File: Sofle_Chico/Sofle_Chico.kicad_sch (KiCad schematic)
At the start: 114 parts, among them J1 Conn_01x05, J2 MJ-4PP-9, J3 Conn_01x04, J4 Conn_01x04, J5 Conn_01x05, J6 Conn_01x05, J7 Conn_01x04, Q1 DMG2305UX, SW1 SW_PUSH, SW10 SW_PUSH, SW11 SW_PUSH, SW12 SW_PUSH, SW13 SW_PUSH, SW14 SW_PUSH, SW15 SW_PUSH, SW16 SW_PUSH, SW17 SW_PUSH, SW18 SW_PUSH, SW19 SW_PUSH, SW2 SW_PUSH, SW20 SW_PUSH, SW21 SW_PUSH, SW22 SW_PUSH, SW23 SW_PUSH, SW24 SW_PUSH, SW25 Rotary_Encoder_Switch-Device, SW26 SW_PUSH, SW27 SW_PUSH, SW28 SW_PUSH, SW29 SW_PUSH, SW3 SW_PUSH, SW30 SW_PUSH, SW4 SW_PUSH, SW5 SW_PUSH, SW6 SW_PUSH, SW7 SW_PUSH, SW8 SW_PUSH, SW9 SW_PUSH, U1 SN74AHCT1G125, U2 Pico

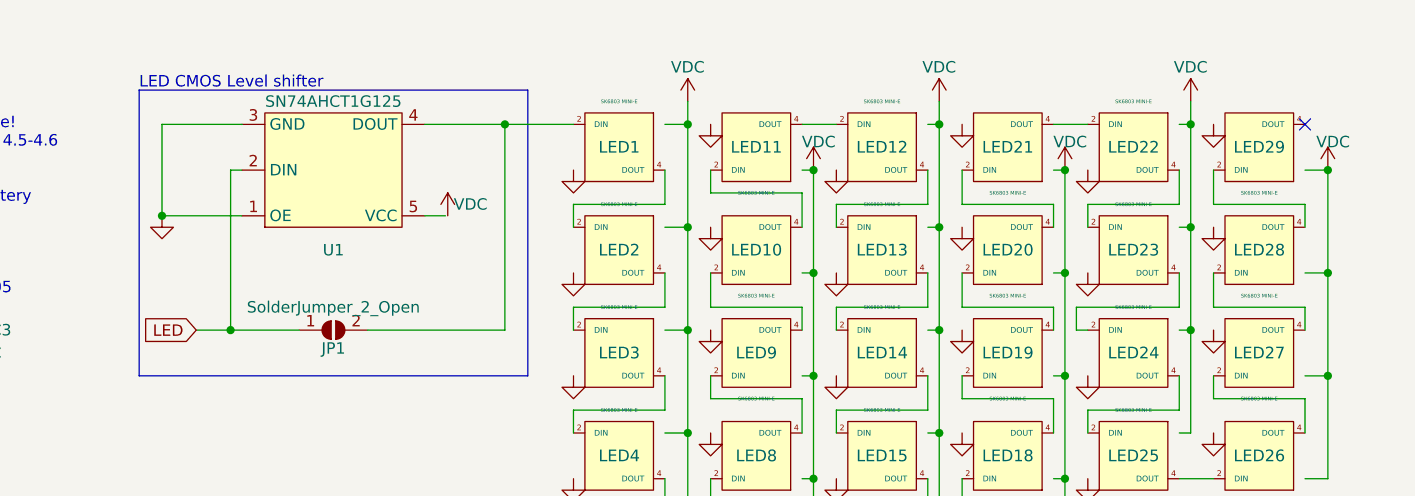
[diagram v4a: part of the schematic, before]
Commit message: Layout progress
LAYOUT PROGRESS
Abandoned Choc V2 support, just aint worth the thru-holes.
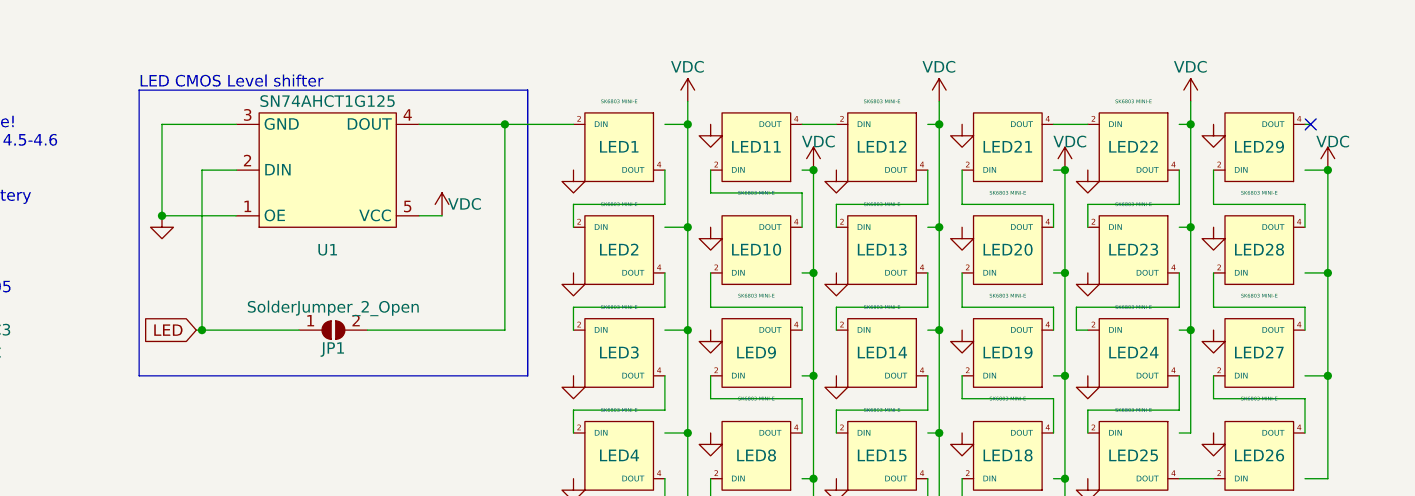
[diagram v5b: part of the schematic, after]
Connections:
- net VDC: now also U1.5 (VCC)
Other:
- moved on the sheet: U1
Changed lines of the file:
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@@
   (junction (at 204.47 123.19) (diameter 0) (color 0 0 0 0)
   )
+  (junction (at 133.985 48.26) (diameter 0) (color 0 0 0 0)
+  )
   (junction (at 215.9 59.69) (diameter 0) (color 0 0 0 0)
   )
@@
   (junction (at 240.03 114.3) (diameter 0) (color 0 0 0 0)
   )
-  (junction (at 137.16 48.26) (diameter 0) (color 0 0 0 0)
-  )
   (junction (at 143.51 139.7) (diameter 0) (color 0 0 0 0)
   )
@@
   (no_connect (at 69.85 166.37))
   (no_connect (at 48.26 78.74))
-  (no_connect (at 256.54 25.4))
+  (no_connect (at 257.175 25.4))
   (wire (pts (xy 214.63 76.2) (xy 218.44 76.2))
     (stroke (width 0) (type default))
@@
     (stroke (width 0) (type default))
   )
-  (wire (pts (xy 137.16 48.26) (xy 133.35 48.26))
+  (wire (pts (xy 133.985 48.26) (xy 144.78 48.26))
     (stroke (width 0) (type default))
   )
@@
     (stroke (width 0) (type default))
   )
-  (wire (pts (xy 137.16 30.48) (xy 137.16 48.26))
+  (wire (pts (xy 133.985 30.48) (xy 133.985 48.26))
     (stroke (width 0) (type default))
   )
@@
     (stroke (width 0) (type default))
   )
-  (wire (pts (xy 129.54 25.4) (xy 138.43 25.4))
+  (wire (pts (xy 129.54 25.4) (xy 137.795 25.4))
     (stroke (width 0) (type default))
   )
@@
     (stroke (width 0) (type default))
   )
+  (wire (pts (xy 158.115 35.56) (xy 160.655 35.56))
+    (stroke (width 0) (type default))
+  )
   (wire (pts (xy 256.54 55.88) (xy 246.38 55.88))
     (stroke (width 0) (type default))
@@
     (stroke (width 0) (type default))
   )
-  (wire (pts (xy 161.036 35.56) (xy 158.75 35.56))
-    (stroke (width 0) (type default))
-  )
   (wire (pts (xy 214.63 53.34) (xy 214.63 57.15))
     (stroke (width 0) (type default))
@@
     (stroke (width 0) (type default))
   )
-  (wire (pts (xy 158.75 25.4) (xy 167.64 25.4))
+  (wire (pts (xy 158.115 25.4) (xy 167.64 25.4))
     (stroke (width 0) (type default))
   )
@@
     (stroke (width 0) (type default))
   )
-  (wire (pts (xy 138.43 30.48) (xy 137.16 30.48))
+  (wire (pts (xy 137.795 30.48) (xy 133.985 30.48))
+    (stroke (width 0) (type default))
+  )
+  (wire (pts (xy 257.175 25.4) (xy 256.54 25.4))
     (stroke (width 0) (type default))
   )
@@
     (stroke (width 0) (type default))
   )
+  (wire (pts (xy 133.985 48.26) (xy 133.35 48.26))
+    (stroke (width 0) (type default))
+  )
   (wire (pts (xy 224.79 139.7) (xy 224.79 156.21))
     (stroke (width 0) (type default))
@@
     (stroke (width 0) (type default))
   )
-  (wire (pts (xy 144.78 48.26) (xy 137.16 48.26))
-    (stroke (width 0) (type default))
-  )
   (wire (pts (xy 219.71 130.81) (xy 240.03 130.81))
     (stroke (width 0) (type default))
@@
     (stroke (width 0) (type default))
   )
-  (wire (pts (xy 129.54 35.56) (xy 138.43 35.56))
+  (wire (pts (xy 129.54 35.56) (xy 137.795 35.56))
     (stroke (width 0) (type default))
   )
@@
     )
   )
-  (symbol (lib_id "Sofle_Pico:SN74AHCT1G125") (at 148.59 30.48 0) (mirror x) (unit 1)
+  (symbol (lib_id "Sofle_Pico:SN74AHCT1G125") (at 147.955 30.48 0) (mirror x) (unit 1)
     (in_bom yes) (on_board yes) (dnp no)
-    (property "Reference" "U1" (at 148.59 39.37 0)
+    (property "Reference" "U1" (at 147.955 39.37 0)
       (effects (font (size 1.27 1.27)))
     )
-    (property "Value" "SN74AHCT1G125" (at 148.59 22.86 0)
+    (property "Value" "SN74AHCT1G125" (at 147.955 22.86 0)
       (effects (font (size 1.27 1.27)))
     )
-    (property "Footprint" "PCM_Package_TO_SOT_SMD_AKL:SOT-23-5_HandSoldering" (at 148.59 20.32 0)
+    (property "Footprint" "PCM_Package_TO_SOT_SMD_AKL:SOT-23-5_HandSoldering" (at 147.955 20.32 0)
       (effects (font (size 1.27 1.27)) hide)
     )
-    (property "Datasheet" "https://www.ti.com/general/docs/suppproductinfo.tsp?distId=26&gotoUrl=http%3A%2F%2Fwww.ti.com%2Flit%2Fgpn%2Fsn74ahct1g125" (at 148.59 16.51 0)
+    (property "Datasheet" "https://www.ti.com/general/docs/suppproductinfo.tsp?distId=26&gotoUrl=http%3A%2F%2Fwww.ti.com%2Flit%2Fgpn%2Fsn74ahct1g125" (at 147.955 16.51 0)
       (effects (font (size 1.27 1.27)) hide)
     )
@@
     )
   )
-  (symbol (lib_id "power:VDC") (at 161.29 35.56 0) (unit 1)
+  (symbol (lib_name "VDC_5") (lib_id "power:VDC") (at 160.655 35.56 0) (unit 1)
     (in_bom yes) (on_board yes) (dnp no) (fields_autoplaced)
-    (property "Reference" "#PWR0110" (at 161.29 39.37 0)
+    (property "Reference" "#PWR0110" (at 160.655 39.37 0)
       (effects (font (size 1.27 1.27)) hide)
     )
-    (property "Value" "VDC" (at 163.83 34.29 0)
+    (property "Value" "VDC" (at 163.195 34.29 0)
       (effects (font (size 1.27 1.27)))
     )
-    (property "Footprint" "" (at 161.29 35.56 0)
+    (property "Footprint" "" (at 160.655 35.56 0)
       (effects (font (size 1.27 1.27)) hide)
     )
-    (property "Datasheet" "" (at 161.29 35.56 0)
+    (property "Datasheet" "" (at 160.655 35.56 0)
       (effects (font (size 1.27 1.27)) hide)
     )

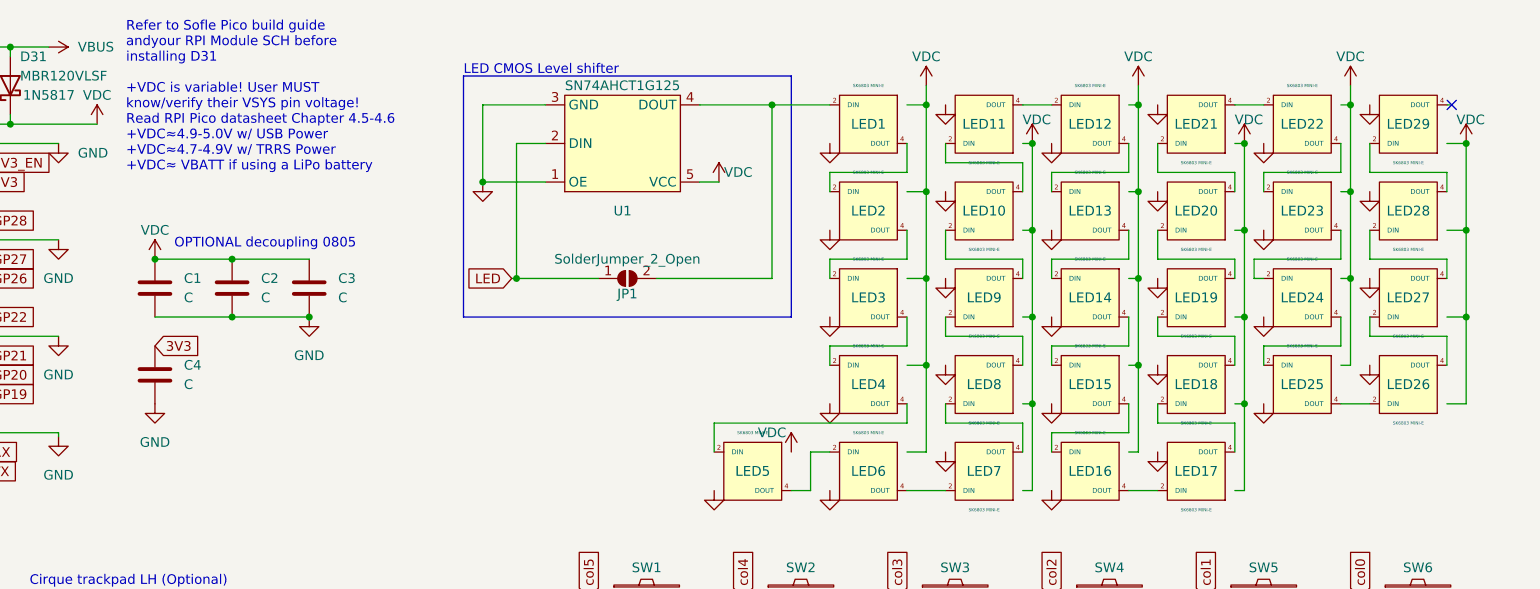
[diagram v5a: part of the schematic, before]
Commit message: progress
Fixing footprints, init routing complete and handling DRCs
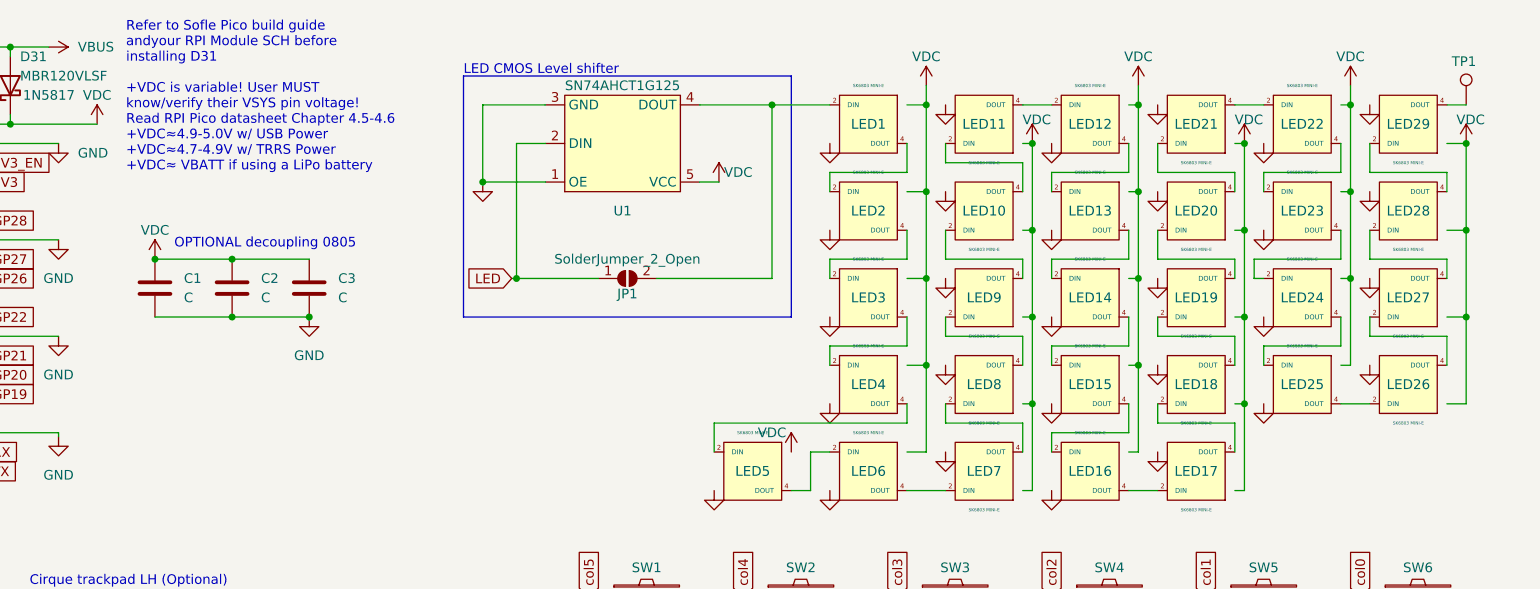
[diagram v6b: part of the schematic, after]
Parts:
- removed C4: C, Capacitor_SMD:C_0805_2012Metric_Pad1.18x1.45mm_HandSolder, symbol Device:C
- added TP1: TestPoint, TestPoint:TestPoint_THTPad_2.0x2.0mm_Drill1.0mm, symbol Connector:TestPoint
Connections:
- net at LED29.4 (DOUT): now also TP1.1
- no-connect marks 8 -> 7
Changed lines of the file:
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@@
   (no_connect (at 69.85 166.37))
   (no_connect (at 48.26 78.74))
-  (no_connect (at 257.175 25.4))
   (wire (pts (xy 214.63 76.2) (xy 218.44 76.2))
     (stroke (width 0) (type default))
@@
     (stroke (width 0) (type default))
   )
+  (wire (pts (xy 256.54 25.4) (xy 259.08 25.4))
+    (stroke (width 0) (type default))
+  )
   (wire (pts (xy 175.26 45.72) (xy 175.26 48.26))
     (stroke (width 0) (type default))
@@
     (stroke (width 0) (type default))
   )
-  (wire (pts (xy 257.175 25.4) (xy 256.54 25.4))
-    (stroke (width 0) (type default))
-  )
   (wire (pts (xy 201.93 64.77) (xy 201.93 53.34))
     (stroke (width 0) (type default))
@@
     )
   )
-  (global_label "3V3" (shape input) (at 86.36 57.15 0) (fields_autoplaced)
-    (effects (font (size 1.27 1.27)) (justify left))
-    (property "Intersheetrefs" "${INTERSHEET_REFS}" (at 92.1192 57.15 0)
-      (effects (font (size 1.27 1.27)) (justify left) hide)
-    )
-  )
   (global_label "SCL" (shape input) (at 69.85 163.83 180) (fields_autoplaced)
     (effects (font (size 1.27 1.27)) (justify right))
@@
     )
   )
-  (symbol (lib_name "GND_5") (lib_id "power:GND") (at 86.36 64.77 0) (unit 1)
-    (in_bom yes) (on_board yes) (dnp no) (fields_autoplaced)
-    (property "Reference" "#PWR025" (at 86.36 71.12 0)
-      (effects (font (size 1.27 1.27)) hide)
-    )
-    (property "Value" "GND" (at 86.36 69.85 0)
-      (effects (font (size 1.27 1.27)))
-    )
-    (property "Footprint" "" (at 86.36 64.77 0)
-      (effects (font (size 1.27 1.27)) hide)
-    )
-    (property "Datasheet" "" (at 86.36 64.77 0)
-      (effects (font (size 1.27 1.27)) hide)
-    )
-    (pin "1")
-    (instances
-      (project "Sofle_Chico"
-        (path "/06057b3a-55ab-4f4e-913e-2aeec5ff3587"
-          (reference "#PWR025") (unit 1)
-        )
-      )
-    )
-  )
   (symbol (lib_name "SK6803MINIE_V2_1") (lib_id "Sofle_Pico:SK6803MINIE_V2") (at 195.58 27.94 180) (unit 1)
     (in_bom yes) (on_board yes) (dnp no)
@@
     )
   )
-  (symbol (lib_id "Device:C") (at 86.36 60.96 0) (unit 1)
-    (in_bom yes) (on_board yes) (dnp no) (fields_autoplaced)
-    (property "Reference" "C4" (at 90.17 59.69 0)
-      (effects (font (size 1.27 1.27)) (justify left))
-    )
-    (property "Value" "C" (at 90.17 62.23 0)
-      (effects (font (size 1.27 1.27)) (justify left))
-    )
-    (property "Footprint" "Capacitor_SMD:C_0805_2012Metric_Pad1.18x1.45mm_HandSolder" (at 87.3252 64.77 0)
-      (effects (font (size 1.27 1.27)) hide)
-    )
-    (property "Datasheet" "~" (at 86.36 60.96 0)
-      (effects (font (size 1.27 1.27)) hide)
-    )
-    (pin "2")
-    (pin "1")
-    (instances
-      (project "Sofle_Chico"
-        (path "/06057b3a-55ab-4f4e-913e-2aeec5ff3587"
-          (reference "C4") (unit 1)
-        )
-      )
-    )
-  )
   (symbol (lib_name "SK6803MINIE_V2_1") (lib_id "Sofle_Pico:SK6803MINIE_V2") (at 195.58 62.23 180) (unit 1)
     (in_bom yes) (on_board yes) (dnp no)
@@
         )
       )
+    )
+  )
+  (symbol (lib_id "Connector:TestPoint") (at 259.08 25.4 0) (unit 1)
+    (in_bom yes) (on_board yes) (dnp no)
+    (property "Reference" "TP1" (at 257.175 19.685 0)
+      (effects (font (size 1.27 1.27)) (justify left))
+    )
+    (property "Value" "TestPoint" (at 260.477 23.3101 0)
+      (effects (font (size 1.27 1.27)) (justify left) hide)
+    )
+    (property "Footprint" "TestPoint:TestPoint_THTPad_2.0x2.0mm_Drill1.0mm" (at 264.16 25.4 0)
+      (effects (font (size 1.27 1.27)) hide)
+    )
+    (property "Datasheet" "~" (at 264.16 25.4 0)
+      (effects (font (size 1.27 1.27)) hide)
+    )
+    (pin "1")
+    (instances
+      (project "Sofle_Chico"
+        (path "/06057b3a-55ab-4f4e-913e-2aeec5ff3587"
+          (reference "TP1") (unit 1)
+        )
+      )
